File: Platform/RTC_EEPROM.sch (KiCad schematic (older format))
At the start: 21 parts, among them U4 DS3231M, U5 AT24CS32-SSHM, U6 MCP7940N-xMS, Y1 32KHz crystal

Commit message: Updated the schematic.
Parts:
- removed C9: 0.1U to 1UF, symbol Device:CP
- removed R22, R23: 2K, symbol Device:R
- removed R24: 10K, symbol Device:R
- removed TP1, TP2: TestPoint, symbol Connector:TestPoint
- removed U4: DS3231M, Package_SO:SOIC-16W_7.5x10.3mm_P1.27mm, symbol Timer_RTC:DS3231M
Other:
- note removed: "Reset pin is internally tied to High and \nrecommended not to use external pullup"
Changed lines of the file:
@@
 $EndDescr
-$Comp
-L Timer_RTC:DS3231M U4
-U 1 1 5FB09C8B
-P 2950 2900
-F 0 "U4" H 2950 2411 50  0000 C CNN
-F 1 "DS3231M" H 2950 2320 50  0000 C CNN
-F 2 "Package_SO:SOIC-16W_7.5x10.3mm_P1.27mm" H 2950 2300 50  0001 C CNN
-F 3 "http://datasheets.maximintegrated.com/en/ds/DS3231.pdf" H 3220 2950 50  0001 C CNN
-	1    2950 2900
-	1    0    0    -1
-$EndComp
-$Comp
-L power:+3.3V #PWR042
-U 1 1 5FB0AC4A
-P 1700 2050
-F 0 "#PWR042" H 1700 1900 50  0001 C CNN
-F 1 "+3.3V" H 1715 2223 50  0000 C CNN
-F 2 "" H 1700 2050 50  0001 C CNN
-F 3 "" H 1700 2050 50  0001 C CNN
-	1    1700 2050
-	1    0    0    -1
-$EndComp
-$Comp
-L power:GND #PWR043
-U 1 1 5FB0AFF3
-P 2950 3900
-F 0 "#PWR043" H 2950 3650 50  0001 C CNN
-F 1 "GND" H 2955 3727 50  0000 C CNN
-F 2 "" H 2950 3900 50  0001 C CNN
-F 3 "" H 2950 3900 50  0001 C CNN
-	1    2950 3900
-	1    0    0    -1
-$EndComp
-Wire Wire Line
-	1700 2050 1700 2250
-Wire Wire Line
-	1700 2250 2200 2250
-Wire Wire Line
-	2850 2250 2850 2500
-Text GLabel 2050 2700 0    50   Input ~ 0
-SCL
-Text GLabel 1400 2950 0    50   Input ~ 0
-SDA
-Wire Wire Line
-	1400 2950 1450 2950
-Wire Wire Line
-	1650 2950 1650 2800
-Wire Wire Line
-	1650 2800 2450 2800
-Wire Wire Line
-	2050 2700 2200 2700
-Wire Wire Line
-	2200 2300 2200 2250
-Connection ~ 2200 2250
-Wire Wire Line
-	2200 2250 2850 2250
-Wire Wire Line
-	2200 2600 2200 2700
-Connection ~ 2200 2700
-Wire Wire Line
-	2200 2700 2450 2700
-$Comp
-L Device:R R22
-U 1 1 5FB0C756
-P 1450 2550
-F 0 "R22" H 1520 2596 50  0000 L CNN
-F 1 "2K" H 1520 2505 50  0000 L CNN
-F 2 "" V 1380 2550 50  0001 C CNN
-F 3 "~" H 1450 2550 50  0001 C CNN
-	1    1450 2550
-	1    0    0    -1
-$EndComp
-Wire Wire Line
-	1450 2700 1450 2950
-Connection ~ 1450 2950
-Wire Wire Line
-	1450 2950 1650 2950
-Wire Wire Line
-	1450 2400 1450 2250
-Wire Wire Line
-	1450 2250 1700 2250
-Connection ~ 1700 2250
-$Comp
-L Device:CP C9
-U 1 1 5FB178E8
-P 950 2400
-F 0 "C9" H 1068 2446 50  0000 L TNN
-F 1 "0.1U to 1UF" H 1068 2355 50  0000 R TNN
-F 2 "" H 988 2250 50  0001 C CNN
-F 3 "~" H 950 2400 50  0001 C CNN
-	1    950  2400
-	1    0    0    -1
-$EndComp
-Wire Wire Line
-	950  2250 1450 2250
-Connection ~ 1450 2250
-$Comp
-L power:GND #PWR041
-U 1 1 5FB1839E
-P 950 2550
-F 0 "#PWR041" H 950 2300 50  0001 C CNN
-F 1 "GND" H 955 2377 50  0000 C CNN
-F 2 "" H 950 2550 50  0001 C CNN
-F 3 "" H 950 2550 50  0001 C CNN
-	1    950  2550
-	1    0    0    -1
-$EndComp
-$Comp
-L Device:R R23
-U 1 1 5FB0BB27
-P 2200 2450
-F 0 "R23" H 2270 2496 50  0000 L CNN
-F 1 "2K" H 2270 2405 50  0000 L CNN
-F 2 "" V 2130 2450 50  0001 C CNN
-F 3 "~" H 2200 2450 50  0001 C CNN
-	1    2200 2450
-	1    0    0    -1
-$EndComp
 $Comp
 L Timer:MCP7940N-xMS U6
@@
 	5350 2450 5600 2450
 Connection ~ 5600 2450
-Text GLabel 3700 3300 2    50   Input ~ 0
-PA27
-Wire Wire Line
-	2950 3300 2950 3900
-$Comp
-L Device:R R24
-U 1 1 5FB4ECAA
-P 3600 3050
-F 0 "R24" H 3670 3096 50  0000 L CNN
-F 1 "10K" H 3670 3005 50  0000 L CNN
-F 2 "" V 3530 3050 50  0001 C CNN
-F 3 "~" H 3600 3050 50  0001 C CNN
-	1    3600 3050
-	1    0    0    -1
-$EndComp
-$Comp
-L power:+3.3V #PWR044
-U 1 1 5FB4F46E
-P 3600 2900
-F 0 "#PWR044" H 3600 2750 50  0001 C CNN
-F 1 "+3.3V" H 3615 3073 50  0000 C CNN
-F 2 "" H 3600 2900 50  0001 C CNN
-F 3 "" H 3600 2900 50  0001 C CNN
-	1    3600 2900
-	1    0    0    -1
-$EndComp
-Wire Wire Line
-	3600 3200 3600 3300
-Wire Wire Line
-	3600 3300 3700 3300
-Wire Wire Line
-	3450 3000 3450 3300
-Wire Wire Line
-	3450 3300 3600 3300
-Connection ~ 3600 3300
 $Comp
 L Memory_EEPROM:AT24CS32-SSHM U5
@@
 	550  1300 550  600
 Wire Notes Line
-	4850 1600 4850 4450
-Wire Notes Line
-	4850 4450 550  4450
-Wire Notes Line
-	550  4450 550  1600
-Wire Notes Line
-	550  1600 4850 1600
-Wire Notes Line
 	4950 950  4950 3850
 Wire Notes Line
@@
 Wire Wire Line
 	7800 1850 7500 1850
-Wire Notes Line
-	2500 3400 2500 4250
-Wire Notes Line
-	2500 4250 600  4250
-Wire Notes Line
-	600  4250 600  3400
-Wire Notes Line
-	600  3400 2500 3400
-Text Notes 800  3850 0    50   ~ 0
-Reset pin is internally tied to High and \nrecommended not to use external pullup
-$Comp
-L Connector:TestPoint TP1
-U 1 1 5FB718D1
-P 1800 3150
-F 0 "TP1" H 1858 3268 50  0000 L CNN
-F 1 "TestPoint" H 1858 3177 50  0000 L CNN
-F 2 "" H 2000 3150 50  0001 C CNN
-F 3 "~" H 2000 3150 50  0001 C CNN
-	1    1800 3150
-	1    0    0    -1
-$EndComp
-Wire Wire Line
-	1800 3150 2450 3150
-Wire Wire Line
-	2450 3150 2450 3100
-$Comp
-L Connector:TestPoint TP2
-U 1 1 5FB7652B
-P 3600 2550
-F 0 "TP2" H 3658 2668 50  0000 L CNN
-F 1 "TestPoint" H 3658 2577 50  0000 L CNN
-F 2 "" H 3800 2550 50  0001 C CNN
-F 3 "~" H 3800 2550 50  0001 C CNN
-	1    3600 2550
-	1    0    0    -1
-$EndComp
-Wire Wire Line
-	3600 2550 3600 2700
-Wire Wire Line
-	3600 2700 3450 2700
 $Comp
 L Device:R_Small R30
@@
 	7500 1300 7500 1450
 Connection ~ 7500 1450
-Text GLabel 3050 2250 2    50   Input ~ 0
-VBAT
-Wire Wire Line
-	3050 2250 2950 2250
-Wire Wire Line
-	2950 2250 2950 2500
 $Comp
 L Device:C_Small C11

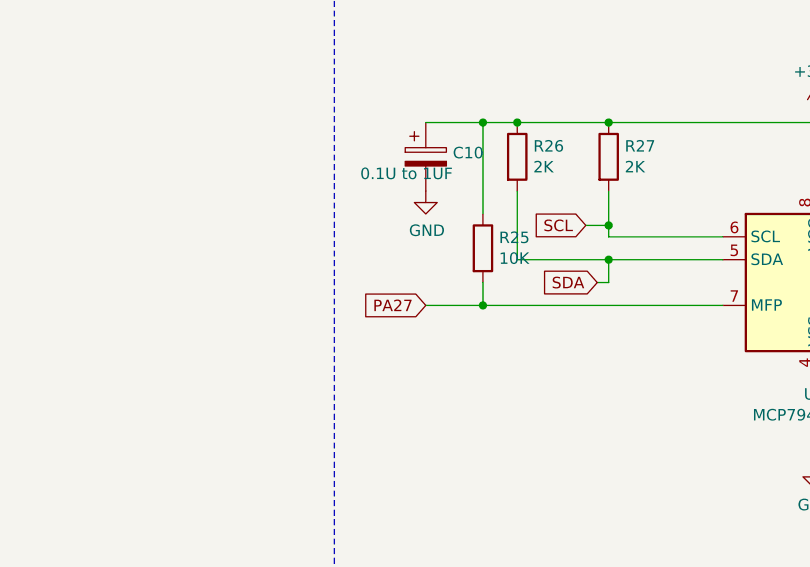
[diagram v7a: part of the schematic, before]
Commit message: updated the schematic as per the latest IO xls.
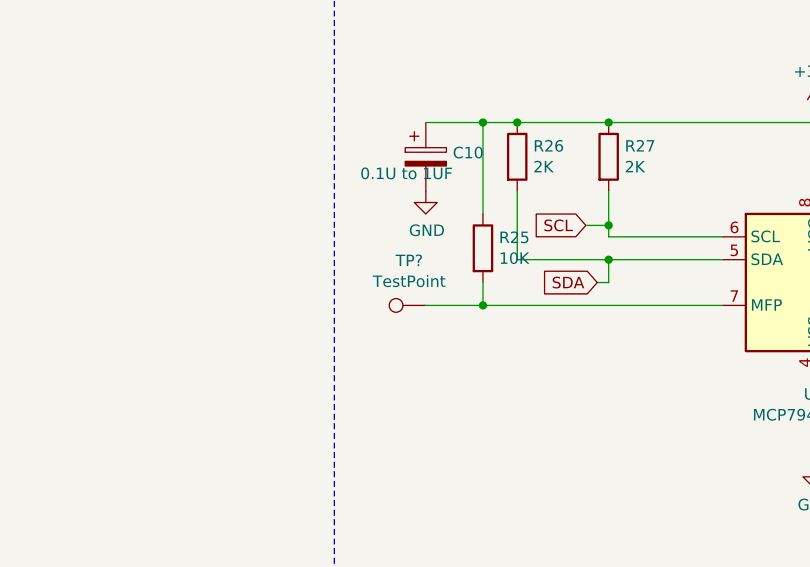
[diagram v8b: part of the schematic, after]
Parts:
- added TP?: TestPoint, symbol Connector:TestPoint
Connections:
- net PA27: no longer names the net of R25.2, U6.7 (MFP)
- net PA27: now also TP?.1
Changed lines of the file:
@@
 Wire Wire Line
 	5600 2450 6650 2450
-Text GLabel 5350 2450 0    50   Input ~ 0
-PA27
-Wire Wire Line
-	5350 2450 5600 2450
-Connection ~ 5600 2450
 $Comp
 L Memory_EEPROM:AT24CS32-SSHM U5
@@
 Wire Wire Line
 	8150 2350 8450 2350
+$Comp
+L Connector:TestPoint TP?
+U 1 1 60677E6E
+P 5350 2450
+F 0 "TP?" V 5545 2522 50  0000 C CNN
+F 1 "TestPoint" V 5454 2522 50  0000 C CNN
+F 2 "" H 5550 2450 50  0001 C CNN
+F 3 "~" H 5550 2450 50  0001 C CNN
+	1    5350 2450
+	0    -1   -1   0
+$EndComp
+Wire Wire Line
+	5350 2450 5600 2450
+Connection ~ 5600 2450
 $EndSCHEMATC
